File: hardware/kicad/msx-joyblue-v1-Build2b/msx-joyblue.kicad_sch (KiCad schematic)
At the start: 39 parts, among them J1 MSX Port1, J2 MSX Port2, J4 I2C, SW1 JOY PWR, SW2 MODE, SW3 SWAP, U1 74LS03, U2 74LS03, U3 ESP32 Kit, U4 74LS03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

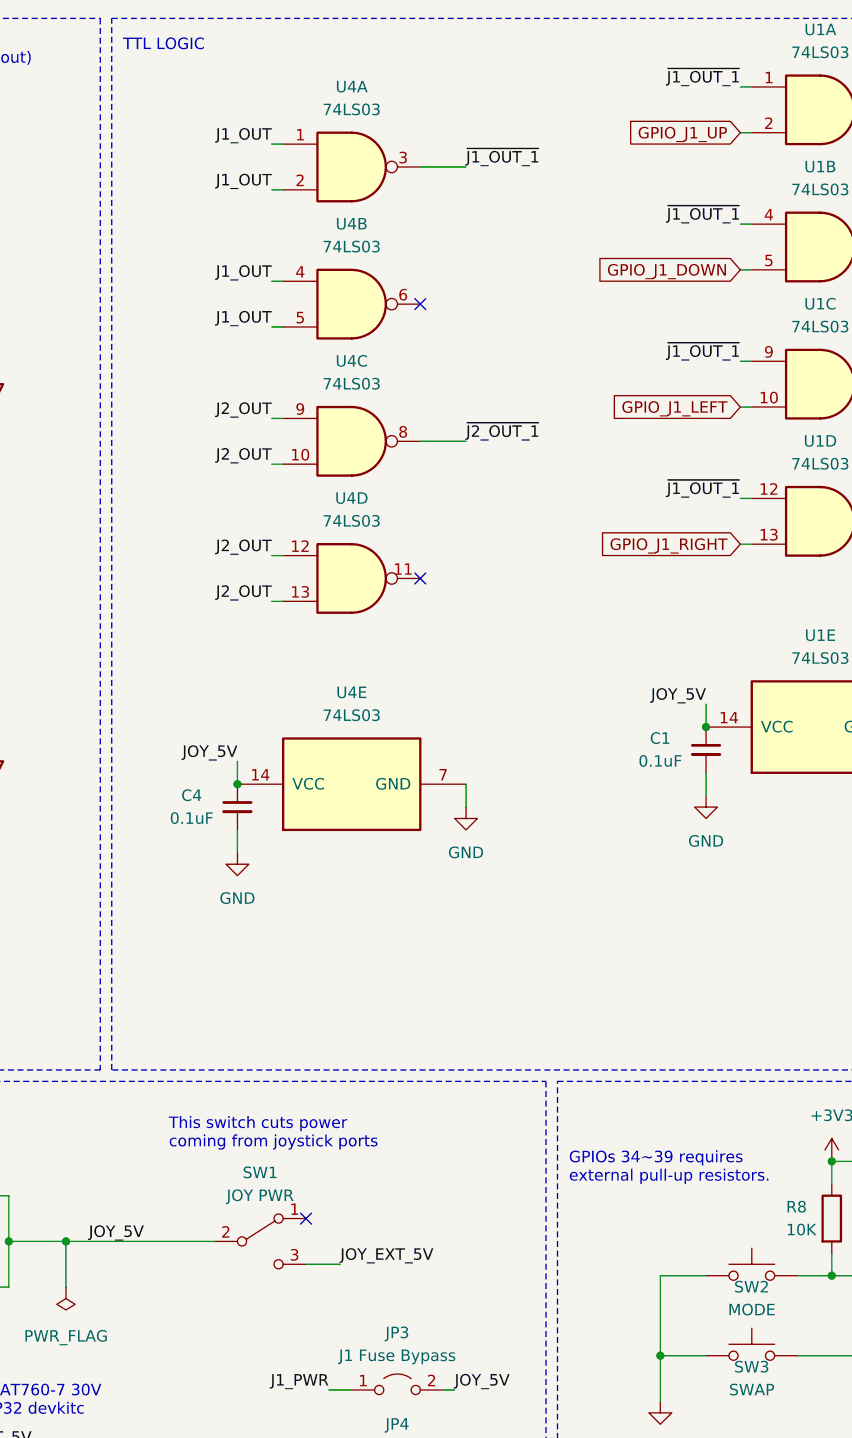
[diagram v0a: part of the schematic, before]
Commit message: hardware: add missing pull-ups to v1 Build2b
Signed-off-by: Albert Herranz <albert_herranz@yahoo.es>
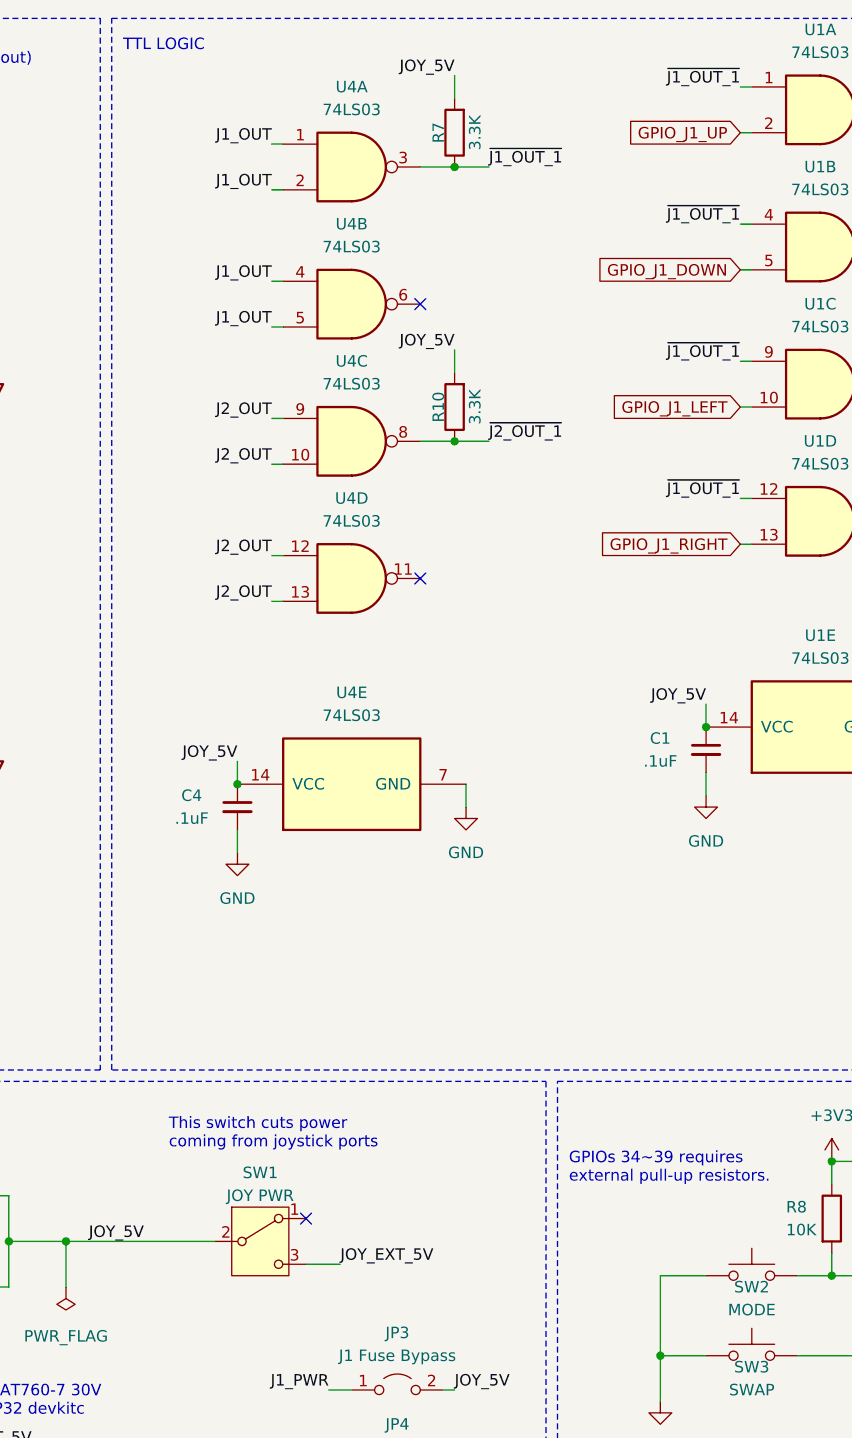
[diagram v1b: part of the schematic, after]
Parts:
- added R10, R7: 3.3K, My_Components:Res_762, symbol Device:R
- C1, C4: value 0.1uF -> .1uF
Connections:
- net JOY_5V: now also R10.2, R7.2
- net ~{J1_OUT_1}: now also R7.1
- net ~{J2_OUT_1}: now also R10.1
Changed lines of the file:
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@@
   (junction (at 71.12 101.6) (diameter 0) (color 0 0 0 0)
   )
+  (junction (at 95.25 63.5) (diameter 0) (color 0 0 0 0)
+  )
   (junction (at 137.16 143.51) (diameter 0) (color 0 0 0 0)
   )
@@
   (junction (at 172.72 95.25) (diameter 0) (color 0 0 0 0)
   )
+  (junction (at 95.25 33.02) (diameter 0) (color 0 0 0 0)
+  )
   (junction (at 142.24 165.1) (diameter 0) (color 0 0 0 0)
   )
@@
     (stroke (width 0) (type default))
   )
+  (wire (pts (xy 95.25 22.86) (xy 95.25 25.4))
+    (stroke (width 0) (type default))
+  )
   (wire (pts (xy 365.76 48.26) (xy 363.22 48.26))
     (stroke (width 0) (type default))
@@
     (stroke (width 0) (type default))
   )
-  (wire (pts (xy 91.44 63.5) (xy 96.52 63.5))
+  (wire (pts (xy 91.44 63.5) (xy 95.25 63.5))
     (stroke (width 0) (type default))
   )
@@
     (stroke (width 0) (type default))
   )
+  (wire (pts (xy 91.44 33.02) (xy 95.25 33.02))
+    (stroke (width 0) (type default))
+  )
   (wire (pts (xy 330.2 96.52) (xy 330.2 101.6))
     (stroke (width 0) (type default))
@@
     (stroke (width 0) (type default))
   )
+  (wire (pts (xy 95.25 53.34) (xy 95.25 55.88))
+    (stroke (width 0) (type default))
+  )
   (wire (pts (xy 76.2 35.56) (xy 74.93 35.56))
     (stroke (width 0) (type default))
@@
     (stroke (width 0) (type default))
   )
+  (wire (pts (xy 95.25 33.02) (xy 99.06 33.02))
+    (stroke (width 0) (type default))
+  )
   (wire (pts (xy 191.77 154.94) (xy 204.47 154.94))
     (stroke (width 0) (type default))
@@
     (stroke (width 0) (type default))
   )
+  (wire (pts (xy 95.25 63.5) (xy 99.06 63.5))
+    (stroke (width 0) (type default))
+  )
   (wire (pts (xy 39.37 38.1) (xy 39.37 53.34))
     (stroke (width 0) (type default))
@@
     (stroke (width 0) (type default))
   )
-  (wire (pts (xy 91.44 33.02) (xy 96.52 33.02))
-    (stroke (width 0) (type default))
-  )
   (wire (pts (xy 53.34 175.26) (xy 48.26 175.26))
     (stroke (width 0) (type default))
@@
     (effects (font (size 1.27 1.27)) (justify right bottom))
   )
+  (label "JOY_5V" (at 95.25 22.86 180) (fields_autoplaced)
+    (effects (font (size 1.27 1.27)) (justify right bottom))
+  )
   (label "JOY_5V" (at 95.25 179.07 0) (fields_autoplaced)
     (effects (font (size 1.27 1.27)) (justify left bottom))
@@
     (effects (font (size 1.27 1.27)) (justify left bottom))
   )
-  (label "~{J1_OUT_1}" (at 96.52 33.02 0) (fields_autoplaced)
+  (label "~{J1_OUT_1}" (at 99.06 33.02 0) (fields_autoplaced)
     (effects (font (size 1.27 1.27)) (justify left bottom))
   )
@@
     (effects (font (size 1.27 1.27)) (justify left bottom))
   )
-  (label "~{J2_OUT_1}" (at 96.52 63.5 0) (fields_autoplaced)
+  (label "~{J2_OUT_1}" (at 99.06 63.5 0) (fields_autoplaced)
     (effects (font (size 1.27 1.27)) (justify left bottom))
   )
@@
     (effects (font (size 1.27 1.27)) (justify right bottom))
   )
+  (label "JOY_5V" (at 95.25 53.34 180) (fields_autoplaced)
+    (effects (font (size 1.27 1.27)) (justify right bottom))
+  )
   (label "~{J2_OUT_1}" (at 176.53 39.37 180) (fields_autoplaced)
     (effects (font (size 1.27 1.27)) (justify right bottom))
@@
       (effects (font (size 1.27 1.27)))
     )
-    (property "Value" "0.1uF" (at 66.04 105.41 0)
+    (property "Value" ".1uF" (at 66.04 105.41 0)
       (effects (font (size 1.27 1.27)))
     )
@@
     )
   )
+  (symbol (lib_id "Device:R") (at 95.25 29.21 180) (unit 1)
+    (in_bom yes) (on_board yes) (dnp no)
+    (property "Reference" "R7" (at 93.472 29.21 90)
+      (effects (font (size 1.27 1.27)))
+    )
+    (property "Value" "3.3K" (at 97.536 29.21 90)
+      (effects (font (size 1.27 1.27)))
+    )
+    (property "Footprint" "My_Components:Res_762" (at 97.028 29.21 90)
+      (effects (font (size 1.27 1.27)) hide)
+    )
+    (property "Datasheet" "~" (at 95.25 29.21 0)
+      (effects (font (size 1.27 1.27)) hide)
+    )
+    (property "LCSC" "C4310" (at 95.25 29.21 90)
+      (effects (font (size 1.27 1.27)) hide)
+    )
+    (pin "1")
+    (pin "2")
+    (instances
+      (project "msx-joyblue"
+        (path "/dc99579c-b122-4cb4-babd-5f1a36d86f4c"
+          (reference "R7") (unit 1)
+        )
+      )
+    )
+  )
   (symbol (lib_id "Connector:DE9_Plug") (at 31.75 102.87 270) (unit 1)
     (in_bom yes) (on_board yes) (dnp no) (fields_autoplaced)
@@
     )
   )
+  (symbol (lib_id "Device:R") (at 95.25 59.69 180) (unit 1)
+    (in_bom yes) (on_board yes) (dnp no)
+    (property "Reference" "R10" (at 93.472 59.69 90)
+      (effects (font (size 1.27 1.27)))
+    )
+    (property "Value" "3.3K" (at 97.536 59.69 90)
+      (effects (font (size 1.27 1.27)))
+    )
+    (property "Footprint" "My_Components:Res_762" (at 97.028 59.69 90)
+      (effects (font (size 1.27 1.27)) hide)
+    )
+    (property "Datasheet" "~" (at 95.25 59.69 0)
+      (effects (font (size 1.27 1.27)) hide)
+    )
+    (property "LCSC" "C4310" (at 95.25 59.69 90)
+      (effects (font (size 1.27 1.27)) hide)
+    )
+    (pin "1")
+    (pin "2")
+    (instances
+      (project "msx-joyblue"
+        (path "/dc99579c-b122-4cb4-babd-5f1a36d86f4c"
+          (reference "R10") (unit 1)
+        )
+      )
+    )
+  )
   (symbol (lib_id "74xx:74LS03") (at 135.89 72.39 0) (unit 4)
     (in_bom yes) (on_board yes) (dnp no)
@@
       (effects (font (size 1.27 1.27)))
     )
-    (property "Value" "0.1uF" (at 118.11 99.06 0)
+    (property "Value" ".1uF" (at 118.11 99.06 0)
       (effects (font (size 1.27 1.27)))
     )
